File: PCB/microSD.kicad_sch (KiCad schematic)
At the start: 7 parts

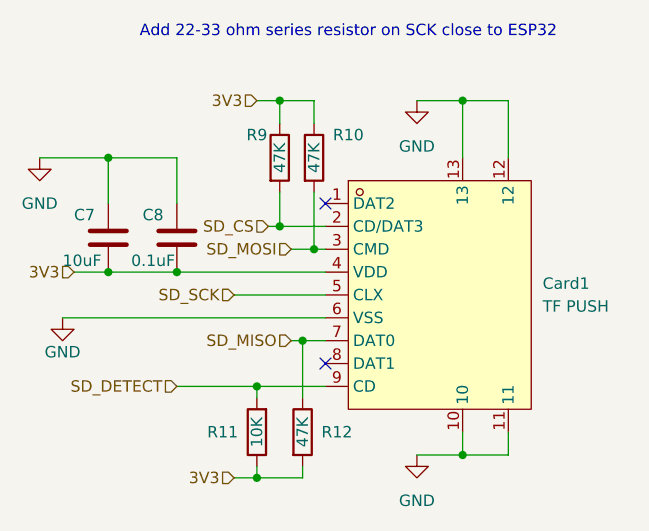
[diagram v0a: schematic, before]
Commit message: microSD card added
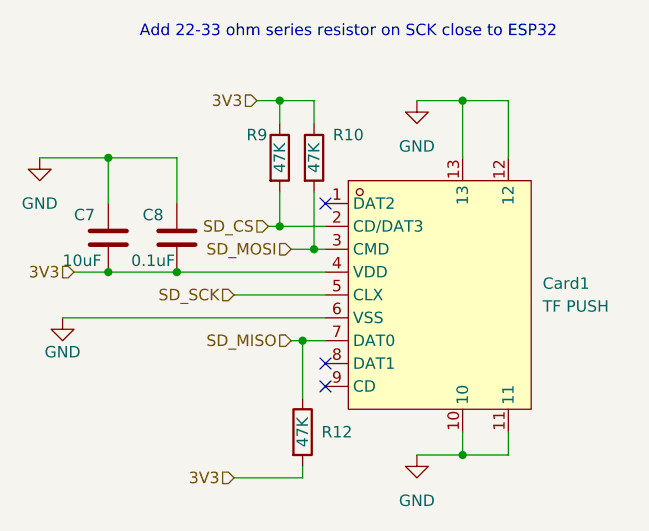
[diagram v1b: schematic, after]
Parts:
- removed R11: 10K, Resistor_SMD:R_0402_1005Metric_Pad0.72x0.64mm_HandSolder, symbol Device:R
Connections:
- net SD_DETECT: no longer names the net of Card1.9 (CD)
- no-connect marks 2 -> 3
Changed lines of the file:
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@@
-	)
-	(junction
-		(at 107.95 97.79)
-		(diameter 0)
-		(color 0 0 0 0)
 	)
 	(junction
@@
 		(color 0 0 0 0)
 	)
-	(junction
-		(at 107.95 107.95)
-		(diameter 0)
-		(color 0 0 0 0)
+	(no_connect
+		(at 115.57 97.79)
 	)
 	(no_connect
@@
 	(wire
 		(pts
-			(xy 105.41 107.95) (xy 107.95 107.95)
-		)
-		(stroke
-			(width 0)
-			(type default)
-		)
-	)
-	(wire
-		(pts
-			(xy 107.95 97.79) (xy 107.95 99.06)
-		)
-		(stroke
-			(width 0)
-			(type default)
-		)
-	)
-	(wire
-		(pts
-			(xy 107.95 97.79) (xy 115.57 97.79)
-		)
-		(stroke
-			(width 0)
-			(type default)
-		)
-	)
-	(wire
-		(pts
 			(xy 114.3 76.2) (xy 114.3 82.55)
 		)
@@
 	(wire
 		(pts
-			(xy 113.03 107.95) (xy 107.95 107.95)
+			(xy 105.41 107.95) (xy 113.03 107.95)
 		)
 		(stroke
@@
 	(wire
 		(pts
-			(xy 99.06 97.79) (xy 107.95 97.79)
-		)
-		(stroke
-			(width 0)
-			(type default)
-		)
-	)
-	(wire
-		(pts
 			(xy 83.82 72.39) (xy 91.44 72.39)
 		)
@@
 	(wire
 		(pts
-			(xy 107.95 106.68) (xy 107.95 107.95)
-		)
-		(stroke
-			(width 0)
-			(type default)
-		)
-	)
-	(wire
-		(pts
 			(xy 110.49 80.01) (xy 115.57 80.01)
 		)
@@
 		(shape input)
 		(at 107.95 66.04 180)
-		(effects
-			(font
-				(size 1.27 1.27)
-			)
-			(justify right)
-		)
-	)
-	(hierarchical_label "SD_DETECT"
-		(shape input)
-		(at 99.06 97.79 180)
 		(effects
 			(font
@@
 					(unit 1)
 				)
-			)
-		)
-	)
-	(symbol
-		(lib_id "Device:R")
-		(at 107.95 102.87 180)
-		(unit 1)
-		(exclude_from_sim no)
-		(in_bom yes)
-		(on_board yes)
-		(dnp no)
-		(property "Reference" "R11"
-			(at 104.14 102.87 0)
-			(effects
-				(font
-					(size 1.27 1.27)
-				)
-			)
-		)
-		(property "Value" "10K"
-			(at 107.95 102.87 90)
-			(effects
-				(font
-					(size 1.27 1.27)
-				)
-			)
-		)
-		(property "Footprint" "Resistor_SMD:R_0402_1005Metric_Pad0.72x0.64mm_HandSolder"
-			(at 109.728 102.87 90)
-			(effects
-				(font
-					(size 1.27 1.27)
-				)
-				(hide yes)
-			)
-		)
-		(property "Datasheet" "~"
-			(at 107.95 102.87 0)
-			(effects
-				(font
-					(size 1.27 1.27)
-				)
-				(hide yes)
-			)
-		)
-		(property "Description" "Resistor"
-			(at 107.95 102.87 0)
-			(effects
-				(font
-					(size 1.27 1.27)
-				)
-				(hide yes)
-			)
-		)
-		(pin "1"
-		)
-		(pin "2"
-		)
-		(instances
-			(project "detentOne"
-				(path "/64c66767-4367-4391-b4db-5d3ae338f23b/71cbbc4b-99b0-4dbc-91fe-1d866024ef70"
-					(reference "R11")
-					(unit 1)
-				)

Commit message: Finished schematic
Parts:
- C7: value 10uF -> 10uF 6.3V
- C8: value 0.1uF -> 0.1uF 6.3V
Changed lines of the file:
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@@
 		(dnp no)
 		(property "Reference" "C8"
-			(at 95.25 78.74 0)
+			(at 99.06 79.248 0)
 			(effects
 				(font
@@
 			)
 		)
-		(property "Value" "0.1uF"
-			(at 93.98 83.82 0)
+		(property "Value" "0.1uF 6.3V"
+			(at 93.218 84.074 0)
 			(effects
 				(font
@@
 		(dnp no)
 		(property "Reference" "C7"
-			(at 87.63 78.74 0)
+			(at 87.63 84.074 0)
 			(effects
 				(font
@@
 			)
 		)
-		(property "Value" "10uF"
-			(at 86.36 83.82 0)
-			(effects
-				(font
+		(property "Value" "10uF 6.3V"
+			(at 86.106 79.248 0)
+			(effects
+				(font

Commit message: final checks for PCB, nearly ready to order v1
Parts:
- R9: value 47K -> 10K
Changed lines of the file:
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@@
 			)
 		)
-		(property "Value" "47K"
+		(property "Value" "10K"
 			(at 110.49 72.39 90)
 			(effects
